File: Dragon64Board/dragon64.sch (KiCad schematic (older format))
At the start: 61 parts, among them IC34 27C128, IC35 74LS00, IC36 74LS02, IC37 27C128, IC38 MC6809E, IC39 6883, IC40 74LS138, J1 ATX, Y1 14.31818Mhz

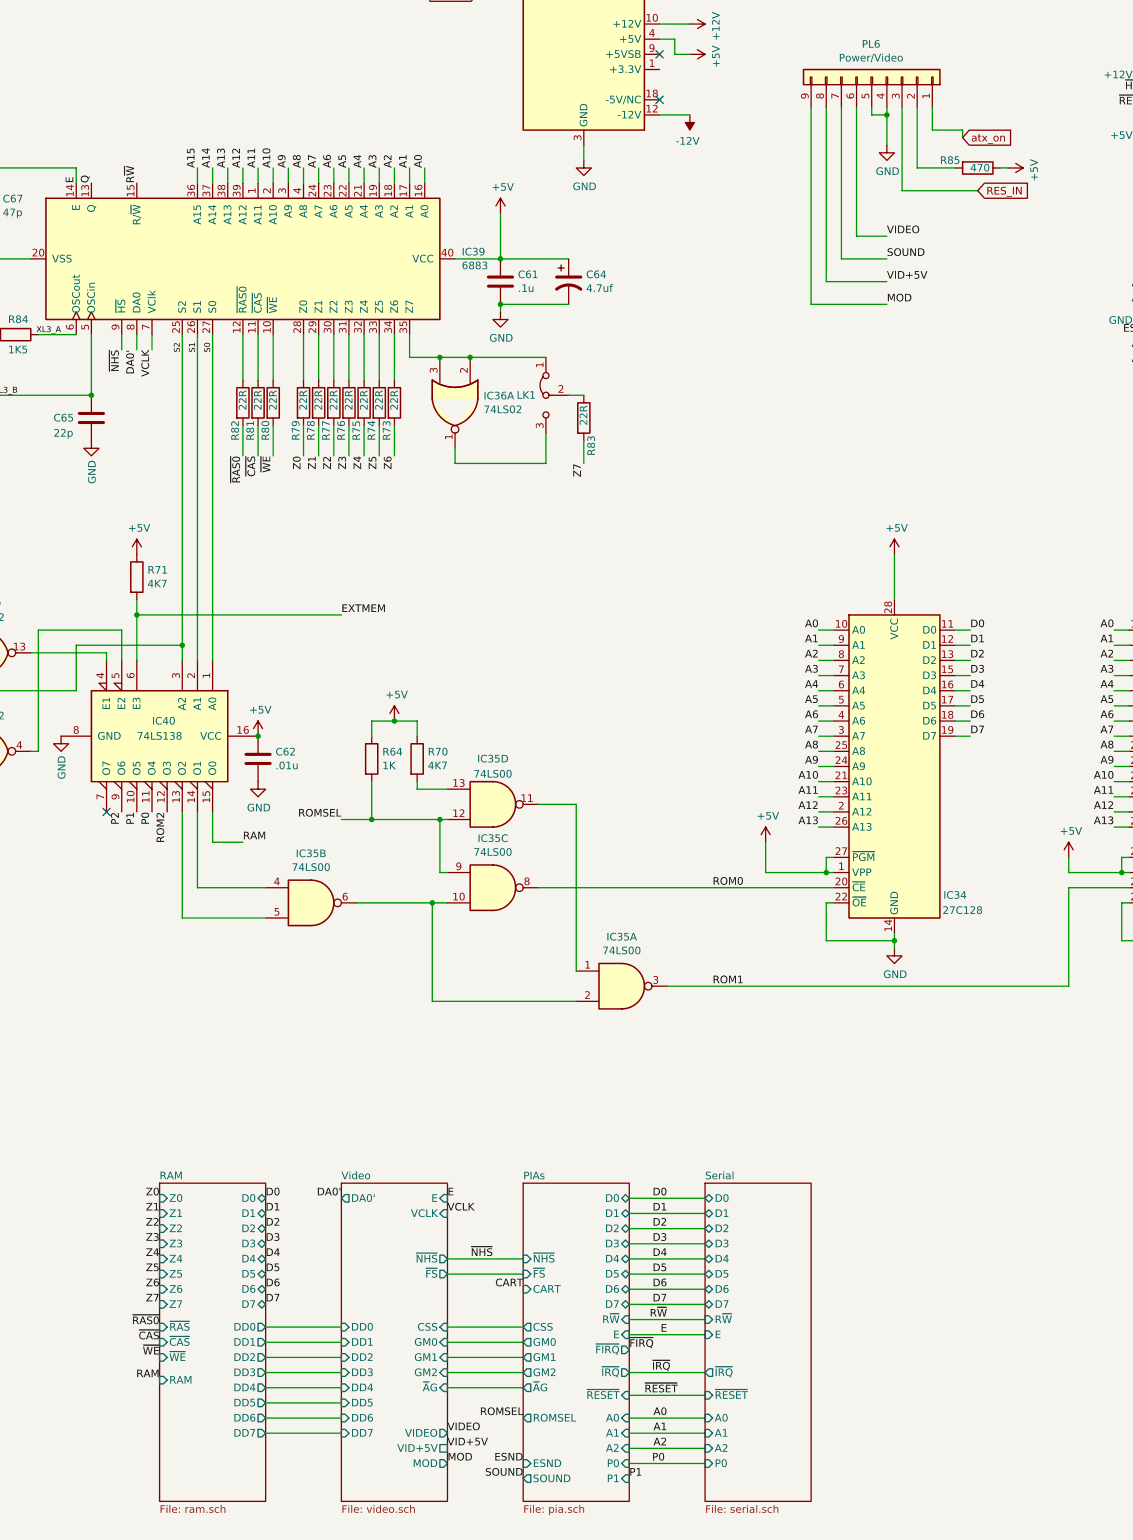
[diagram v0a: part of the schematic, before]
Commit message: PAL to NTSC
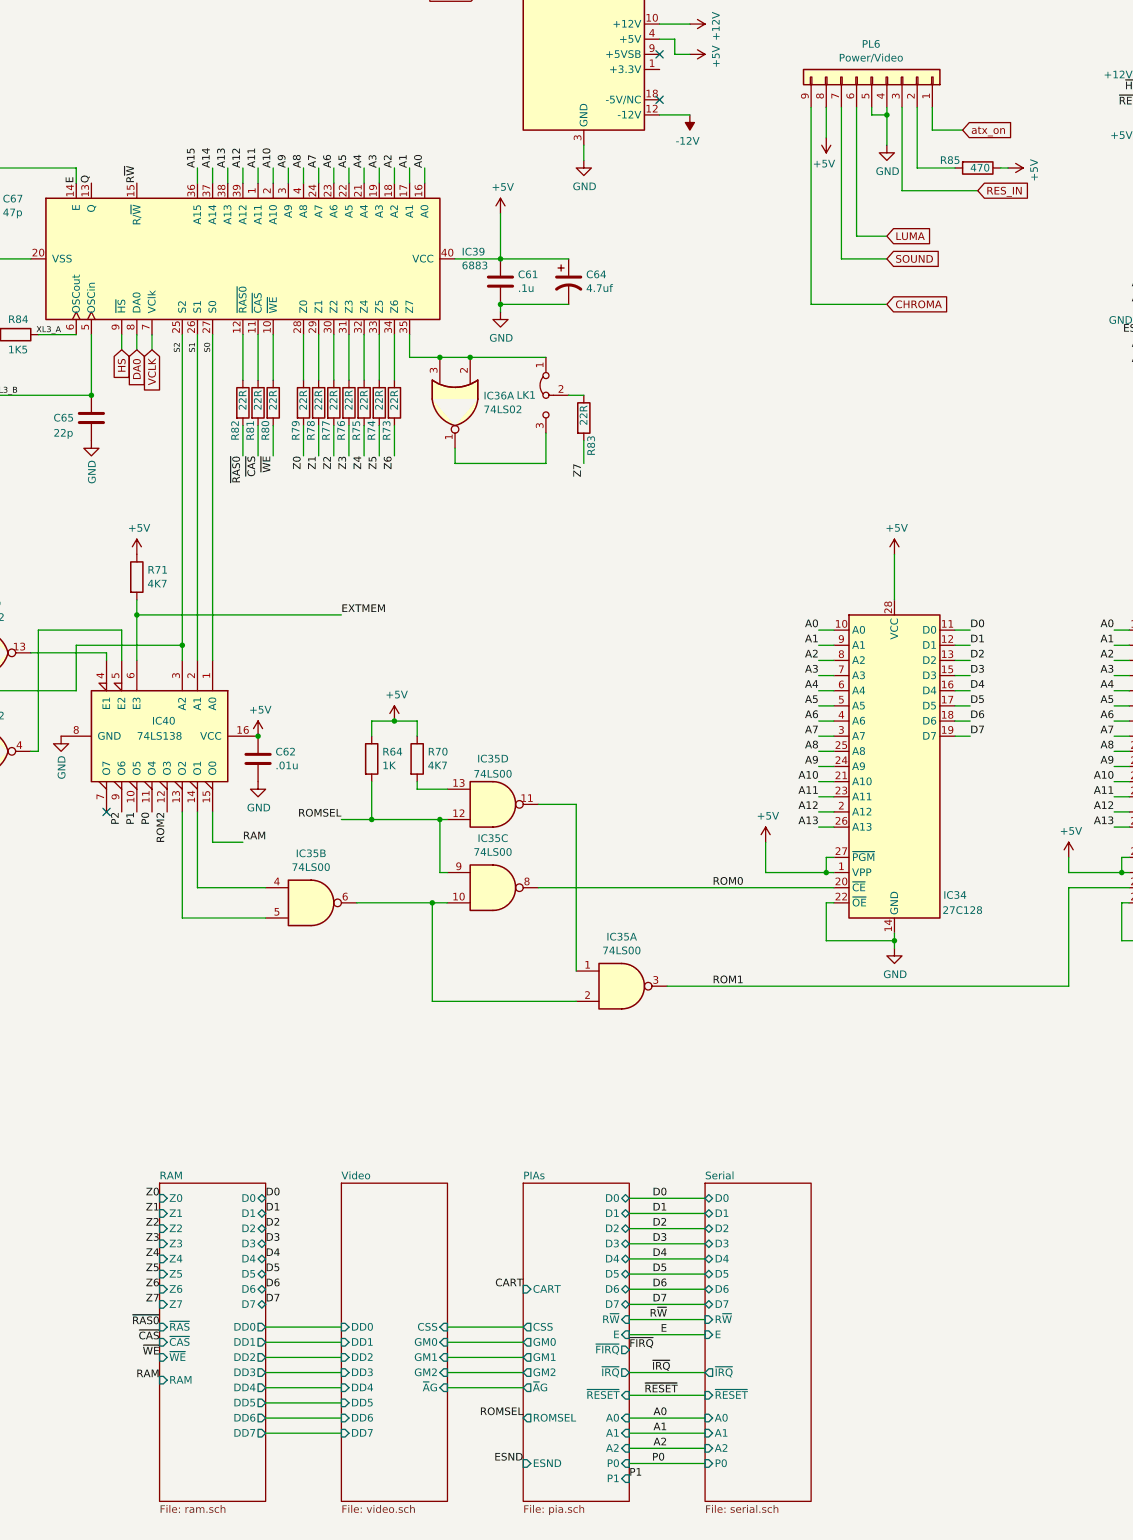
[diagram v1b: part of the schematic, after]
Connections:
- net labels added: CHROMA, DA0, HS, LUMA
- net labels removed: DA0', MOD, VID+5V, VIDEO, ~NHS
- wire segments 322 -> 318
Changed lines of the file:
@@
 Text Label 7750 9550 0    50   ~ 0
 D7
-Text Label 6900 3250 3    50   ~ 0
-DA0'
-Text Label 8250 8850 2    50   ~ 0
-DA0'
 Text Label 7800 3950 3    50   ~ 0
 ~WE
@@
 Text Label 9450 10300 2    50   ~ 0
 ROMSEL
-Text Label 9250 9250 2    50   ~ 0
-~NHS
-Text Label 8950 8850 0    50   ~ 0
-E
 Wire Wire Line
 	10150 10000 10650 10000
@@
 Text Label 10250 10150 0    50   ~ 0
 ~RESET
-Text Label 7000 3250 3    50   ~ 0
-VCLK
-Text Label 6800 3250 3    50   ~ 0
-~NHS
 $Sheet
 S 8250 8750 700  2100
@@
 F8 "DD6" I L 8250 10300 50
 F9 "DD7" I L 8250 10400 50
-F10 "DA0'" O L 8250 8850 50
-F11 "CSS" I R 8950 9700 50
-F12 "GM0" I R 8950 9800 50
-F13 "GM1" I R 8950 9900 50
-F14 "GM2" I R 8950 10000 50
-F15 "~A~G" I R 8950 10100 50
-F16 "~NHS" O R 8950 9250 50
-F17 "E" I R 8950 8850 50
-F18 "VCLK" I R 8950 8950 50
-F19 "~FS" O R 8950 9350 50
-F20 "VIDEO" O R 8950 10400 50
-F21 "MOD" O R 8950 10600 50
-F22 "VID+5V" U R 8950 10500 50
+F10 "CSS" I R 8950 9700 50
+F11 "GM0" I R 8950 9800 50
+F12 "GM1" I R 8950 9900 50
+F13 "GM2" I R 8950 10000 50
+F14 "~A~G" I R 8950 10100 50
 $EndSheet
-Text Label 8950 8950 0    50   ~ 0
-VCLK
-Wire Wire Line
-	8950 9250 9450 9250
-Wire Wire Line
-	8950 9350 9450 9350
 Wire Wire Line
 	7400 6300 7400 6500
@@
 F19 "~FIRQ" O R 10150 9850 50
 F20 "ROMSEL" O L 9450 10300 50
-F21 "~NHS" I L 9450 9250 50
-F22 "~FS" I L 9450 9350 50
-F23 "CART" I L 9450 9450 50
-F24 "~RESET" I R 10150 10150 50
-F25 "P0" I R 10150 10600 50
-F26 "P1" I R 10150 10700 50
-F27 "SOUND" O L 9450 10700 50
-F28 "ESND" I L 9450 10600 50
-F29 "R~W~" I R 10150 9650 50
-F30 "E" I R 10150 9750 50
+F21 "CART" I L 9450 9450 50
+F22 "~RESET" I R 10150 10150 50
+F23 "P0" I R 10150 10600 50
+F24 "P1" I R 10150 10700 50
+F25 "ESND" I L 9450 10600 50
+F26 "R~W~" I R 10150 9650 50
+F27 "E" I R 10150 9750 50
 $EndSheet
 Wire Wire Line
@@
 Wire Wire Line
 	11350 2950 11850 2950
-Text Label 11850 2650 0    50   ~ 0
-SOUND
-Text Label 11850 2500 0    50   ~ 0
-VIDEO
-Text Label 11850 2950 0    50   ~ 0
-MOD
-Text Label 8950 10400 0    50   ~ 0
-VIDEO
-Text Label 8950 10600 0    50   ~ 0
-MOD
-Text Label 9450 10700 2    50   ~ 0
-SOUND
 Text Label 9450 10600 2    50   ~ 0
 ESND
@@
 Wire Wire Line
 	8600 5700 8450 5700
-Text Label 11850 2800 0    50   ~ 0
-VID+5V
-Wire Wire Line
-	11850 2800 11450 2800
-Wire Wire Line
-	11450 2800 11450 1650
-Text Label 8950 10500 0    50   ~ 0
-VID+5V
 Text Label 6400 3150 2    39   ~ 0
 XL3_A
@@
 Wire Wire Line
 	12150 1800 12350 1800
-Wire Wire Line
-	12350 1800 12350 1850
-Text GLabel 12350 1850 2    50   Input ~ 0
+Text GLabel 12350 1800 2    50   Input ~ 0
 atx_on
 Wire Wire Line
@@
 	0    1    1    0
 $EndComp
+Text GLabel 6900 3250 3    50   Input ~ 0
+DA0
+Text GLabel 7000 3250 3    50   Input ~ 0
+VCLK
+Text GLabel 6800 3250 3    50   Input ~ 0
+HS
+Text GLabel 11850 2500 2    50   Input ~ 0
+LUMA
+Text GLabel 11850 2950 2    50   Input ~ 0
+CHROMA
+Wire Wire Line
+	11450 1650 11450 1850
+$Comp
+L power:+5V #PWR0169
+U 1 1 6320476A
+P 11450 1850
+F 0 "#PWR0169" H 11450 1700 50  0001 C CNN
+F 1 "+5V" H 11465 2023 50  0000 C CNN
+F 2 "" H 11450 1850 50  0001 C CNN
+F 3 "" H 11450 1850 50  0001 C CNN
+	1    11450 1850
+	-1   0    0    1
+$EndComp
+Text GLabel 11850 2650 2    50   Input ~ 0
+SOUND
 $EndSCHEMATC

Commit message: Bug fixes and add Floppy Controller
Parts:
- removed C55: 33uf 16V, Capacitor_THT:CP_Radial_D4.0mm_P2.00mm, symbol Device:C_Polarized_US
- removed C65: 22p, Capacitor_THT:C_Disc_D7.5mm_W2.5mm_P5.00mm, symbol Device:C
- removed C70, C71: 1uf, Capacitor_THT:CP_Radial_D4.0mm_P2.00mm, symbol Device:C_Polarized_US
- removed D10, D19, D9: 1N914, Diode_THT:D_DO-35_SOD27_P7.62mm_Horizontal, symbol Device:D
- removed R84: 1K5, Resistor_THT:R_Axial_DIN0207_L6.3mm_D2.5mm_P7.62mm_Horizontal, symbol Device:R
- removed REG1: LM79L05_TO92, Package_TO_SOT_THT:TO-92, symbol Regulator_Linear:LM79L05_TO92
- removed Y1: 14.31818Mhz, Crystal:Crystal_HC49-U_Vertical, symbol Device:Crystal
- added C48: 1u, Capacitor_THT:C_Disc_D7.5mm_W2.5mm_P5.00mm, symbol Device:C
- added D6, D7: 1N4148, Diode_THT:D_DO-35_SOD27_P7.62mm_Horizontal, symbol Device:D
- added R42: 100K, Resistor_THT:R_Axial_DIN0207_L6.3mm_D2.5mm_P7.62mm_Horizontal, symbol Device:R
- added X1: 14.31818Mhz, Package_DIP:DIP-14_W7.62mm_Socket_LongPads, symbol Oscillator:CXO_DIP14
- C8: value .1u -> 1u
- D11: value 1N914 -> 1N4148
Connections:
- net labels removed: -5V, XL3_A, XL3_B, XL3_C
- wire segments 318 -> 323
- no-connect marks 9 -> 10
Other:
- note removed: "16V ELECTRO"
- moved on the sheet: C8, D11, R17

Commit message: enclosure
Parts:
- removed PL7: Cartridge, dragon64:Edge_2x20_P2.54mm_Horizontal, symbol Connector_Generic:Conn_02x20_Odd_Even
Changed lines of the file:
@@
 	1    0    0    -1
-$EndComp
-$Comp
-L Connector_Generic:Conn_02x20_Odd_Even PL7
-U 1 1 5FE1E7FB
-P 13800 2350
-F 0 "PL7" H 13850 3467 50  0000 C CNN
-F 1 "Cartridge" H 13850 3376 50  0000 C CNN
-F 2 "dragon64:Edge_2x20_P2.54mm_Horizontal" H 13800 2350 50  0001 C CNN
-F 3 "~" H 13800 2350 50  0001 C CNN
-	1    13800 2350
-	1    0    0    -1
-$EndComp
-$Comp
-L power:+12V #PWR0119
-U 1 1 5FE249E1
-P 13600 1450
-F 0 "#PWR0119" H 13600 1300 50  0001 C CNN
-F 1 "+12V" V 13615 1578 50  0000 L CNN
-F 2 "" H 13600 1450 50  0001 C CNN
-F 3 "" H 13600 1450 50  0001 C CNN
-	1    13600 1450
-	0    -1   -1   0
-$EndComp
-$Comp
-L power:+12V #PWR0120
-U 1 1 5FE25101
-P 14100 1450
-F 0 "#PWR0120" H 14100 1300 50  0001 C CNN
-F 1 "+12V" V 14115 1578 50  0000 L CNN
-F 2 "" H 14100 1450 50  0001 C CNN
-F 3 "" H 14100 1450 50  0001 C CNN
-	1    14100 1450
-	0    1    1    0
-$EndComp
-$Comp
-L power:+5V #PWR0121
-U 1 1 5FE29844
-P 13600 1850
-F 0 "#PWR0121" H 13600 1700 50  0001 C CNN
-F 1 "+5V" V 13615 1978 50  0000 L CNN
-F 2 "" H 13600 1850 50  0001 C CNN
-F 3 "" H 13600 1850 50  0001 C CNN
-	1    13600 1850
-	0    -1   -1   0
-$EndComp
-$Comp
-L power:GND #PWR0122
-U 1 1 5FE99438
-P 13600 3050
-F 0 "#PWR0122" H 13600 2800 50  0001 C CNN
-F 1 "GND" V 13605 2922 50  0000 R CNN
-F 2 "" H 13600 3050 50  0001 C CNN
-F 3 "" H 13600 3050 50  0001 C CNN
-	1    13600 3050
-	0    1    1    0
-$EndComp
-$Comp
-L power:GND #PWR0123
-U 1 1 5FE9A14D
-P 14100 3050
-F 0 "#PWR0123" H 14100 2800 50  0001 C CNN
-F 1 "GND" V 14105 2922 50  0000 R CNN
-F 2 "" H 14100 3050 50  0001 C CNN
-F 3 "" H 14100 3050 50  0001 C CNN
-	1    14100 3050
-	0    -1   -1   0
 $EndComp
 Connection ~ 6900 5000
@@
 Text Label 8250 5000 0    50   ~ 0
 EXTMEM
-Text Label 14100 3350 0    50   ~ 0
-EXTMEM
-Text Label 14100 2850 0    50   ~ 0
-A11
-Text Label 14100 2750 0    50   ~ 0
-A9
-Text Label 14100 2650 0    50   ~ 0
-A7
-Text Label 14100 2550 0    50   ~ 0
-A5
-Text Label 14100 2450 0    50   ~ 0
-A3
-Text Label 14100 2350 0    50   ~ 0
-A1
-Text Label 14100 2250 0    50   ~ 0
-R~W~
-Text Label 13600 2350 2    50   ~ 0
-A0
-Text Label 13600 2450 2    50   ~ 0
-A2
-Text Label 13600 2550 2    50   ~ 0
-A4
-Text Label 13600 2650 2    50   ~ 0
-A6
-Text Label 13600 2750 2    50   ~ 0
-A8
-Text Label 13600 2850 2    50   ~ 0
-A10
-Text Label 13600 2950 2    50   ~ 0
-A12
-Text Label 13600 3250 2    50   ~ 0
-A13
-Text Label 13600 3350 2    50   ~ 0
-A15
-Text Label 13600 3150 2    50   ~ 0
-ESND
-Text Label 14100 3150 0    50   ~ 0
-P2
-Text Label 14100 3250 0    50   ~ 0
-A14
-Text Label 14100 2950 0    50   ~ 0
-ROM2
-Text Label 14100 1550 0    50   ~ 0
-~NMI
-Text Label 14100 1650 0    50   ~ 0
-E
-Text Label 14100 1750 0    50   ~ 0
-CART
-Text Label 13600 1650 2    50   ~ 0
-~RESET
-Text Label 13600 1550 2    50   ~ 0
-~HALT
-Text Label 13600 1750 2    50   ~ 0
-Q
-Text Label 13600 1950 2    50   ~ 0
-D1
-Text Label 13600 2050 2    50   ~ 0
-D3
-Text Label 13600 2150 2    50   ~ 0
-D5
-Text Label 13600 2250 2    50   ~ 0
-D7
-Text Label 14100 1850 0    50   ~ 0
-D0
-Text Label 14100 1950 0    50   ~ 0
-D2
-Text Label 14100 2050 0    50   ~ 0
-D4
-Text Label 14100 2150 0    50   ~ 0
-D6
 Text Label 10400 8850 2    50   ~ 0
 D0
@@
 Wire Wire Line
 	7600 1800 7600 2150
-Text GLabel 14300 1750 2    50   Input ~ 0
-CART
 Text GLabel 15650 1800 2    50   Input ~ 0
 CART
 Wire Wire Line
 	15650 1800 15450 1800
-Wire Wire Line
-	14300 1750 14100 1750
-Text GLabel 14300 1650 2    50   Input ~ 0
-E
 Text GLabel 15650 1700 2    50   Input ~ 0
 E
 Wire Wire Line
 	15650 1700 15450 1700
-Wire Wire Line
-	14300 1650 14100 1650
-Wire Wire Line
-	13600 1750 13350 1750
-Wire Wire Line
-	13600 1650 13350 1650
-Text GLabel 13350 1750 0    50   Input ~ 0
+Text GLabel 14600 1800 0    50   Input ~ 0
 Q
-Text GLabel 13350 1650 0    50   Input ~ 0
+Text GLabel 14600 1700 0    50   Input ~ 0
 ~RESET
-Text GLabel 14250 2250 2    50   Input ~ 0
+Text GLabel 15650 2300 2    50   Input ~ 0
 R~W~
-Wire Wire Line
-	14250 2250 14100 2250
-Wire Wire Line
-	14300 3150 14100 3150
-Text GLabel 14300 3150 2    50   Input ~ 0
+Text GLabel 15700 3200 2    50   Input ~ 0
 P2
 Text GLabel 15650 1600 2    50   Input ~ 0
@@
 Text GLabel 15700 3000 2    50   Input ~ 0
 ROM2
+Wire Wire Line
+	15450 2300 15650 2300
+Wire Wire Line
+	15450 3200 15700 3200
+Wire Wire Line
+	14950 1700 14600 1700
+Wire Wire Line
+	14950 1800 14600 1800
 $EndSCHEMATC

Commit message: add rom images
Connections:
- net -12V: no longer names the net of J1.12 (-12V)
- no-connect marks 10 -> 12
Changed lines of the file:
@@
-$EndComp
-$Comp
-L power:-12V #PWR0255
-U 1 1 60A525E9
-P 10550 1700
-F 0 "#PWR0255" H 10550 1800 50  0001 C CNN
-F 1 "-12V" H 10565 1873 50  0000 C CNN
-F 2 "" H 10550 1700 50  0001 C CNN
-F 3 "" H 10550 1700 50  0001 C CNN
-	1    10550 1700
-	-1   0    0    1
 $EndComp
 $Comp
@@
 	10450 1300 10550 1300
 Wire Wire Line
-	10350 1700 10550 1700
-Wire Wire Line
 	9850 1900 9850 2000
 Wire Wire Line
@@
 Wire Wire Line
 	14950 1800 14600 1800
+NoConn ~ 10350 1400
+NoConn ~ 10350 1700
+Wire Wire Line
+	15450 1900 15650 1900
+Wire Wire Line
+	15450 2000 15650 2000
+Wire Wire Line
+	15450 2100 15650 2100
+Wire Wire Line
+	15450 2200 15650 2200
+Text GLabel 15650 1900 2    50   Input ~ 0
+D0
+Text GLabel 15650 2000 2    50   Input ~ 0
+D2
+Text GLabel 15650 2100 2    50   Input ~ 0
+D4
+Text GLabel 15650 2200 2    50   Input ~ 0
+D6
+Text GLabel 14600 2000 0    50   Input ~ 0
+D1
+Text GLabel 14600 2100 0    50   Input ~ 0
+D3
+Text GLabel 14600 2200 0    50   Input ~ 0
+D5
+Text GLabel 14600 2300 0    50   Input ~ 0
+D7
+Wire Wire Line
+	14950 2000 14600 2000
+Wire Wire Line
+	14950 2100 14600 2100
+Wire Wire Line
+	14950 2200 14600 2200
+Wire Wire Line
+	14950 2300 14600 2300
 $EndSCHEMATC

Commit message: PCB updates
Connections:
- net +3V3: now reaches J1.1 (+3.3V), J1.11 (+3.3V), J1.2 (+3.3V)
- no-connect marks 12 -> 11
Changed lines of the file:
@@
 Wire Wire Line
 	14950 1800 14600 1800
-NoConn ~ 10350 1400
 NoConn ~ 10350 1700
 Wire Wire Line
@@
 Wire Wire Line
 	14950 2300 14600 2300
+Wire Wire Line
+	10350 1400 10600 1400
+Wire Wire Line
+	10600 1400 10600 1500
+Wire Wire Line
+	10600 1500 10650 1500
+$Comp
+L power:+3.3V #PWR0119
+U 1 1 631AAD95
+P 10650 1500
+F 0 "#PWR0119" H 10650 1350 50  0001 C CNN
+F 1 "+3.3V" V 10665 1628 50  0000 L CNN
+F 2 "" H 10650 1500 50  0001 C CNN
+F 3 "" H 10650 1500 50  0001 C CNN
+	1    10650 1500
+	0    1    1    0
+$EndComp
 $EndSCHEMATC
